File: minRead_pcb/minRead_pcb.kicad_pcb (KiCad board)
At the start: 2 copper layers, 64 x 109.5 mm, 76 parts, among them J1 USB_C_Receptacle, J3 Conn_01x24, J5 Conn_01x02, J7 Micro_SD_Card, Q3 IRLML6402, Q4 Si1308EDL, Q5 AO3401A, Q6 SS8050, SW1 SW_Push, SW12 SW_Push, SW2 SW_Push, SW3 SW_Push, SW4 SW_Push, SW5 SW_Push, SW6 SW_Push, SW7 SW_Push, U2 BQ24074RGT, U3 AP2112K-3.3, U4 ESP32-S3-WROOM-1

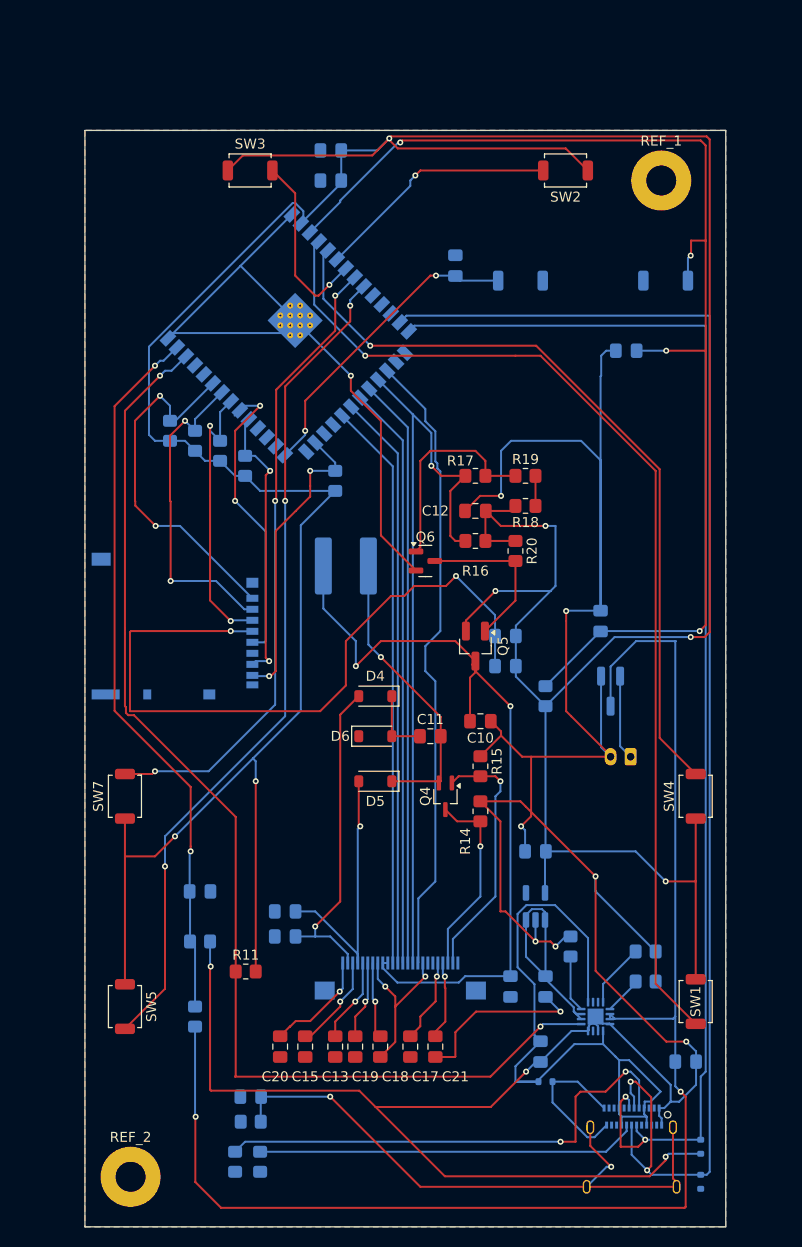
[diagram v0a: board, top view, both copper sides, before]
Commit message: - schematic updates: - usb500 mode enabled on bq - charge limit set to 100mA 8.9kohm (safe for small batteries) - series resistors on sd card and epd lines - esd arrays for usb-c and sd-card - increased output cap for ldo from 4.7u to 22u - added pgood to gpio - confirmed reverse polarity stuff - cap to ground instead of series for sd card vdd - fixed cap values on epd
new layout:
- adjusted board size
- very compact
- need to fill ground planes and check drc errors (a lot because of solder mask)
- need to adjust jst footprint in case there's a better choice
- review review review
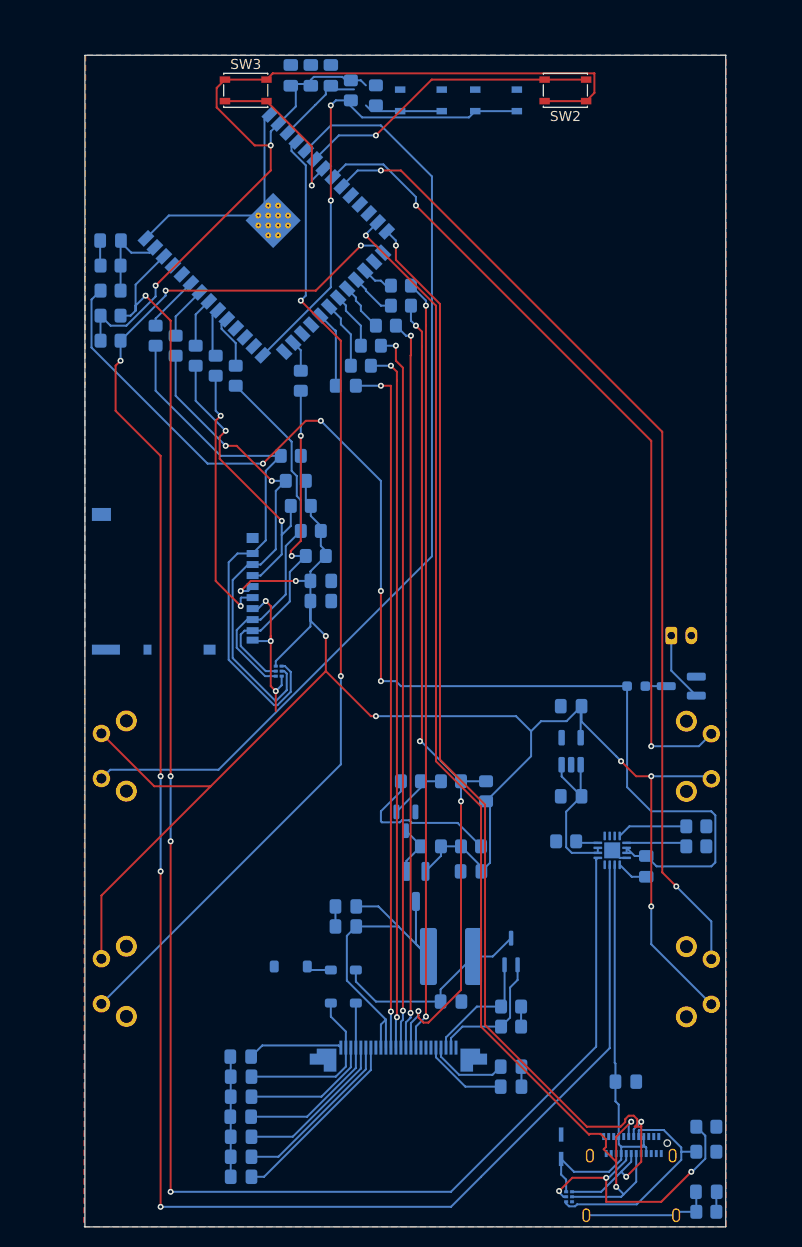
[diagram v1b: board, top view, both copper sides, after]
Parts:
- removed C34, C35: 0.1u, Capacitor_SMD:C_0805_2012Metric_Pad1.18x1.45mm_HandSolder
- removed D1, D2, D3: ESD5Zxx, Diode_SMD:D_SOD-523
- removed REF_1, REF_2: MountingHole_3mm_Pad, MountingHole:MountingHole_3mm_Pad
- added CR1: TSD05CDYFR, footprints:TVS_SOD2_DYF_TEX-M, B.Cu at (155.0, 144.5)
- added R13: 10k, Resistor_SMD:R_0805_2012Metric_Pad1.20x1.40mm_HandSolder, B.Cu at (134.0, 39.0)
- added R21: 33, Resistor_SMD:R_0805_2012Metric_Pad1.20x1.40mm_HandSolder, B.Cu at (122.5, 67.5)
- added R22: 33, Resistor_SMD:R_0805_2012Metric_Pad1.20x1.40mm_HandSolder, B.Cu at (129.0, 68.0)
- added R23: 33, Resistor_SMD:R_0805_2012Metric_Pad1.20x1.40mm_HandSolder, B.Cu at (114.5, 63.5)
- added R24: 33, Resistor_SMD:R_0805_2012Metric_Pad1.20x1.40mm_HandSolder, B.Cu at (116.5, 64.5)
- added R25: 33, Resistor_SMD:R_0805_2012Metric_Pad1.20x1.40mm_HandSolder, B.Cu at (120.5, 66.5)
- added R26: 33, Resistor_SMD:R_0805_2012Metric_Pad1.20x1.40mm_HandSolder, B.Cu at (118.5, 65.5)
- added R27: 0, Resistor_SMD:R_0603_1608Metric_Pad0.98x0.95mm_HandSolder, B.Cu at (162.5, 98.5)
- added R28: 1.1k, Resistor_SMD:R_0805_2012Metric_Pad1.20x1.40mm_HandSolder, B.Cu at (110.0, 64.0)
- added R29: 33, Resistor_SMD:R_0805_2012Metric_Pad1.20x1.40mm_HandSolder, B.Cu at (139.0, 58.5)
- added R30: 33, Resistor_SMD:R_0805_2012Metric_Pad1.20x1.40mm_HandSolder, B.Cu at (139.0, 60.5)
- added R31: 33, Resistor_SMD:R_0805_2012Metric_Pad1.20x1.40mm_HandSolder, B.Cu at (137.5, 62.5)
- added R32: 33, Resistor_SMD:R_0805_2012Metric_Pad1.20x1.40mm_HandSolder, B.Cu at (136.0, 64.5)
- added R33: 33, Resistor_SMD:R_0805_2012Metric_Pad1.20x1.40mm_HandSolder, B.Cu at (135.0, 66.5)
- added R34: 33, Resistor_SMD:R_0805_2012Metric_Pad1.20x1.40mm_HandSolder, B.Cu at (133.5, 68.5)
- added U1: TPD4E004DRYR, TPD4E004DRYR:PSON50P145X100X60-6N, B.Cu at (126.8, 97.0)
- added U5: TPD4E004DRYR, TPD4E004DRYR:PSON50P145X100X60-6N, B.Cu at (155.8, 149.5)
- C10, C11, C12, C13, C15, C17, D4, D5, D6, Q4, Q5, Q6, R11, R14, R15, R16, R17, R18, R19, R20: moved to B.Cu
- C18, C19, C20, C21: value 0.1u -> 1u; moved to B.Cu
- C22, C5: value 0.1u -> 1u
- C6: value 4.7u -> 22u
- J3: footprint custom:24pin0.5mm -> sfv24r:AMPHENOL_SFV24R-2STE1HLF
- R5: value 890 -> 8.9k
- SW1, SW4, SW5, SW7: footprint Button_Switch_SMD:SW_SPST_TS-1088-xR025 -> Button_Switch_THT:SW_Tactile_SPST_Angled_PTS645Vx39-2LFS; moved to B.Cu
- SW12, SW6: footprint Button_Switch_SMD:SW_SPST_TS-1088-xR020 -> Button_Switch_SMD:SW_SPST_PTS810
- SW2, SW3: footprint Button_Switch_SMD:SW_SPST_TS-1088-xR025 -> Button_Switch_SMD:SW_SPST_PTS810
- moved R12 73.0 mm to (110.0, 59.0), turned to 0 degrees
- moved R10 68.1 mm to (110.0, 56.5), turned to 180 degrees
- moved R11 66.9 mm to (110.0, 61.5), turned to 180 degrees
- moved C8 65.6 mm to (110.0, 54.0), turned to 180 degrees
- moved R7 62.3 mm to (136.5, 39.5), turned to -90 degrees
- moved C5 60.8 mm to (132.0, 37.5)
- moved SW4 59.7 mm to (109.1, 103.2), turned to -90 degrees
- moved SW1 59.5 mm to (109.1, 125.7)
- moved SW7 58.6 mm to (170.0, 107.8)
- moved SW5 58.6 mm to (170.0, 130.3), turned to 90 degrees
- moved R2 47.1 mm to (169.5, 145.0), turned to 0 degrees
- moved C1 46.5 mm to (169.5, 149.0), turned to 0 degrees
- moved R1 46.4 mm to (169.5, 151.0), turned to 180 degrees
- moved R3 44.7 mm to (169.5, 142.5), turned to 0 degrees
- moved L1 40.4 mm to (144.0, 125.5)
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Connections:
- net Net-(J1-CC1) renamed /USBC_Power_Native/USBC_CC1
- net Net-(J1-CC2) renamed /USBC_Power_Native/USBC_CC2
- C36 pad 1: 3V3 -> GND
- C36 pad 2: Net-(J7-VDD) -> 3V3
- C37 pad 1: 3V3 -> GND
- C37 pad 2: Net-(J7-VDD) -> 3V3
- J7 pad 1: SD_DAT2 -> Net-(J7-DAT2)
- J7 pad 2: SD_DAT3 -> Net-(J7-DAT3/CD)
- J7 pad 3: SD_CMD -> Net-(J7-CMD)
- J7 pad 4: Net-(J7-VDD) -> 3V3
- J7 pad 5: SD_CLK -> Net-(J7-CLK)
- J7 pad 7: SD_DAT0 -> Net-(J7-DAT0)
- J7 pad 8: SD_DAT1 -> Net-(J7-DAT1)
- Q3 pad 3: VBat+ -> Net-(Q3-D)
- Q4 pad 2: Net-(D5-K) -> /E_ink_HAT/RESE
- Q4 pad 3: /E_ink_HAT/RESE -> Net-(D5-K)
- R53 pad 1: SD_CMD -> Net-(J7-DAT2)
- R54 pad 1: SD_DAT0 -> Net-(J7-DAT3/CD)
- R55 pad 1: SD_DAT1 -> Net-(J7-CMD)
- R8 pad 1: SD_DAT2 -> Net-(J7-DAT0)
- R9 pad 1: SD_DAT3 -> Net-(J7-DAT1)
- U2 pad 5: USB_VBUS -> GND
- U2 pad 6: GND -> USB_VBUS
- U2 pad 7: unconnected-(U2-~{PGOOD}-Pad7) -> PGOOD
- U4 pad 13: ESP32_DP -> ESP32_DN
- U4 pad 14: ESP32_DN -> ESP32_DP
- U4 pad 15: unconnected-(U4-IO3-Pad15) -> PGOOD
- U4 pad 17: EPD_BUSY -> Net-(U4-IO9)
- U4 pad 18: EPD_RST -> Net-(U4-IO10)
- U4 pad 19: EPD_DC -> Net-(U4-IO11)
- U4 pad 20: EPD_CS -> Net-(U4-IO12)
- U4 pad 21: EPD_SCK -> Net-(U4-IO13)
- U4 pad 22: EPD_MOSI -> Net-(U4-IO14)
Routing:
- net GND: track 424.7 -> 67.9 mm, vias 14 -> 3
- net PGOOD: track 0.00 -> 189.0 mm, vias 0 -> 6
- net ESP32_EN: track 122.6 -> 17.2 mm, vias 4 -> 0
- net 3V3: track 390.8 -> 290.1 mm, vias 7 -> 9
- net Net-(J7-VDD): track 73.1 -> 0.00 mm, vias 2 -> 0
- net BAT_MONIT: track 72.0 -> 9.31 mm, vias 2 -> 0
- net Net-(J7-DAT2): track 0.00 -> 54.9 mm
- net CHG_STATUS: track 116.5 -> 168.2 mm, vias 2 -> 4
- net Net-(J7-DAT3/CD): track 0.00 -> 49.0 mm, vias 0 -> 2
- net Net-(J1-SHIELD): track 62.0 -> 13.1 mm, vias 2 -> 0
- net /E_ink_HAT/VCC_EPD_OUT: track 79.9 -> 36.6 mm, vias 2 -> 0
- net Net-(J7-DAT0): track 0.00 -> 37.4 mm
- net Net-(J7-DAT1): track 0.00 -> 35.5 mm, vias 0 -> 2
- net SD_DAT2: track 36.3 -> 5.69 mm, vias 2 -> 0
- net Net-(J7-CMD): track 0.00 -> 30.0 mm, vias 0 -> 2
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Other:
- board size 64 x 109.5 mm -> 64 x 117 mm
- board text added: "BOOT"
- board text added: "RST"

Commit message: draft new rev compact as possible confirmed reverse polarity circuit but need to double check jst connector made sure buttons were as evenly spaced as possible need to ensure every cap is 25v tolerant just as a default all resistors and caps are 0805 maybe double check inductor to see if we can find a better one all decoupling caps are local to their respective component updated 3d models
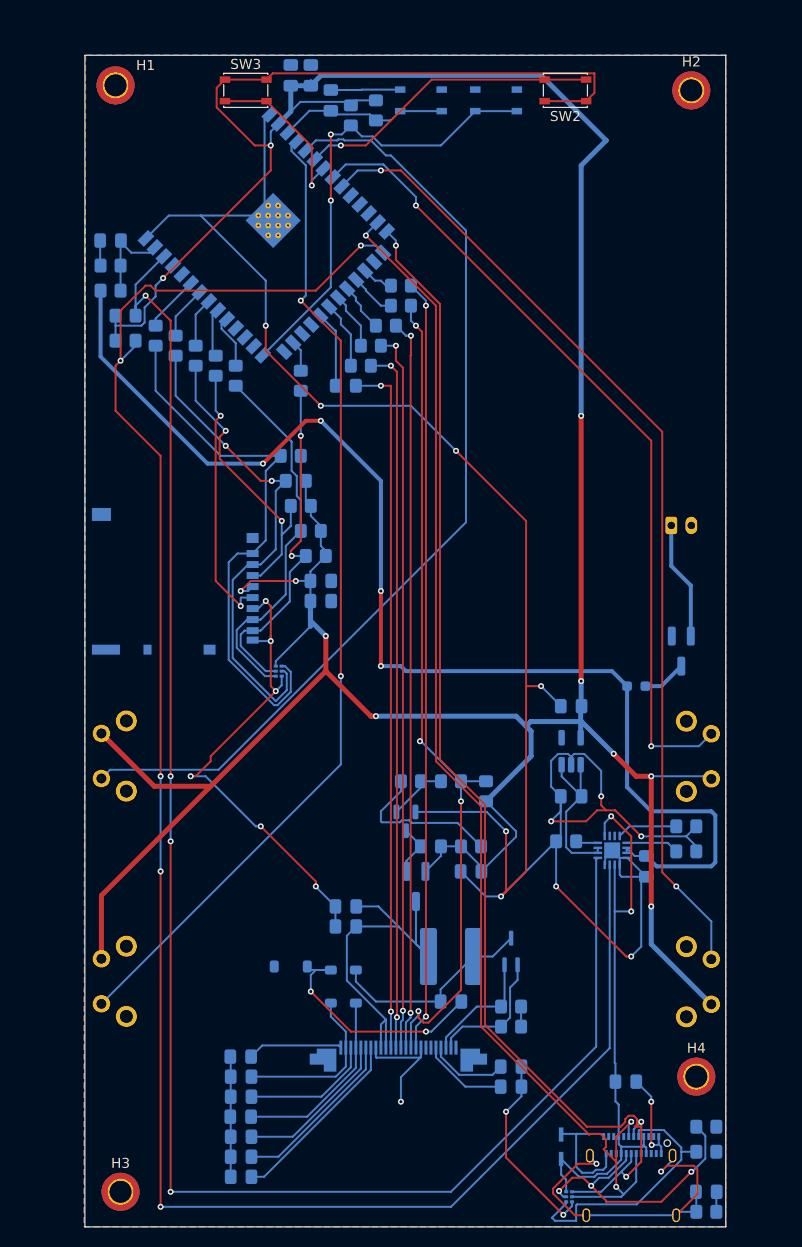
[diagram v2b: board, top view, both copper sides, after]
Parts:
- added H1: MountingHole_Pad, MountingHole:MountingHole_2.2mm_M2_DIN965_Pad_TopBottom, F.Cu at (110.5, 38.5)
- added H2: MountingHole_Pad, MountingHole:MountingHole_2.2mm_M2_DIN965_Pad_TopBottom, F.Cu at (168.0, 39.0)
- added H3: MountingHole_Pad, MountingHole:MountingHole_2.2mm_M2_DIN965_Pad_TopBottom, F.Cu at (111.0, 149.0)
- added H4: MountingHole_Pad, MountingHole:MountingHole_2.2mm_M2_DIN965_Pad_TopBottom, F.Cu at (168.5, 137.5)
- moved J5 11.0 mm to (166.0, 82.5)
- moved Q3 3.50 mm to (167.0, 95.0), turned to -90 degrees
- moved C5 2.50 mm to (132.0, 40.0)
- moved R13 2.50 mm to (134.0, 41.5)
- moved R11 1.50 mm to (111.5, 61.5)
- moved R28 1.50 mm to (111.5, 64.0)
- moved R7 1.50 mm to (136.5, 41.0)
- moved R6 1.12 mm to (167.5, 115.0)
- moved R5 1.00 mm to (167.5, 112.5)
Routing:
- net GND: track 67.9 -> 347.7 mm, vias 3 -> 22
- net 3V3: track 290.1 -> 386.2 mm, vias 9 -> 11
- net Net-(J1-SHIELD): track 13.1 -> 35.8 mm, vias 0 -> 2
- net Net-(D4-K): track 2.49 -> 22.8 mm, vias 0 -> 2
- net USB_VBUS: track 44.5 -> 59.1 mm, vias 0 -> 2
- net /USBC_Power_Native/USBC_CC1: track 22.0 -> 27.0 mm
- net Net-(J5-Pin_1): track 7.04 -> 11.9 mm
- net PGOOD: track 189.0 -> 193.5 mm, vias 6 -> 5
- net Net-(Q3-D): track 2.09 -> 4.42 mm
- net CHG_STATUS: track 168.2 -> 166.5 mm
- net VBat+: track 123.9 -> 122.2 mm
- net ESP32_IO0: track 47.6 -> 46.1 mm
- net Net-(U2-ISET): track 7.05 -> 6.05 mm
- net Net-(U2-TS): track 6.11 -> 5.31 mm

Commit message: draft1.0
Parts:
- Q6: footprint Package_TO_SOT_SMD:SOT-23 -> Package_TO_SOT_SMD:SOT-23_Handsoldering
- R27: footprint Resistor_SMD:R_0603_1608Metric_Pad0.98x0.95mm_HandSolder -> Resistor_SMD:R_0805_2012Metric_Pad1.20x1.40mm_HandSolder

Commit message: - fixed diode orientation of eink booster - everything works except eink driver: - rst pin pulls high, dc doesn't toggle, etc etc. - TODO for next rev: - remove reset stabilizer and just route 3v3 to epd inductor circuit - replace esd arrays with hand-solderable components (qfn to sot) - replace buttons with resistor ladder circuit (xteink-like) - replace bq24074 with more discrete charging circuit to aid hand-solder - add led driver (15v to 7 series LEDs) - replace usb-c receptacle with through-hole - add external dupont pins for external LED driver access and spare GPIOs
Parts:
- added G***: LOGO, LOGO, F.Cu at (140.0, 87.5)
- moved D6 1.50 mm to (128.0, 125.0)
- moved Q6 1.50 mm to (138.0, 112.0)
- moved L1 1.00 mm to (144.0, 124.5)
- moved D4 0.50 mm to (131.5, 128.5)
- turned D5 to 90 degrees
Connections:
- C11 pad 2: Net-(D5-K) -> Net-(D5-A)
- D5 pad 1: Net-(D5-K) -> /E_ink_HAT/PREVGH
- D5 pad 2: /E_ink_HAT/PREVGH -> Net-(D5-A)
- J5 pad 1: Net-(J5-Pin_1) -> GND
- J5 pad 2: GND -> Net-(J5-Pin_2)
- L1 pad 2: Net-(D5-K) -> Net-(D5-A)
- Q3 pad 2: Net-(J5-Pin_1) -> Net-(J5-Pin_2)
- Q4 pad 3: Net-(D5-K) -> Net-(D5-A)
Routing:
- net Net-(D5-K): track 20.8 -> 0.00 mm
- net Net-(D5-A): track 0.00 -> 20.1 mm
- net GND: track 347.7 -> 361.2 mm, vias 22 -> 29
- net Net-(J5-Pin_1): track 11.9 -> 0.00 mm
- net Net-(J5-Pin_2): track 0.00 -> 11.1 mm
- net Net-(R18-Pad1): track 16.2 -> 25.2 mm
- net Net-(D4-K): track 22.8 -> 28.3 mm
- net Net-(Q5-G): track 5.36 -> 7.09 mm
- net /E_ink_HAT/VCC_EPD_OUT: track 36.6 -> 38.0 mm
- net Net-(Q6-B): track 6.08 -> 6.99 mm
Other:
- board text added: "for safety please do not charge via usbc-pd try to stay in 5V range (from generic wall charger or pc usb port)"
- board text added: "place 24-pin eink header here pls"
- board text added: "place esp32-s3 here pls"
- board text added: "place sd card here pls"
